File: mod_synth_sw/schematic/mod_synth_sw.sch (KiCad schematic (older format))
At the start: 43 parts, among them J1 Conn_02x08_Odd_Even, J2 CLK, J3 RST, J4 I/O, J5 I/O 1, J6 I/O 2, J7 I/O 3, J8 I/O 4, Q1 2N3904, Q2 2N3904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

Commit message: Layout some tracks
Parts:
- added C2, C3, C4: 100nf, Capacitor_THT:C_Disc_D9.0mm_W2.5mm_P5.00mm, symbol Device:C_Small
- added C5, C6: 10uf, Capacitor_THT:CP_Radial_D5.0mm_P2.00mm, symbol Device:CP_Small
- added J10, J9: Conn_01x05_Female, Connector_PinSocket_2.54mm:PinSocket_1x05_P2.54mm_Vertical, symbol Connector:Conn_01x05_Female
- added J11, J12: Conn_01x05_Male, Connector_PinHeader_2.54mm:PinHeader_1x05_P2.54mm_Vertical, symbol Connector:Conn_01x05_Male
- U1: footprint Package_DIP:DIP-16_W7.62mm -> Package_DIP:DIP-16_W7.62mm_Socket_LongPads
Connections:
- net +12V: now also J1.10 (Pin_10), J1.9 (Pin_9), U1.13 (V+), U2.16 (VDD), C2.2, C4.2, C6.1
- net GND: now also J1.3 (Pin_3), J1.5 (Pin_5), J1.7 (Pin_7), U1.5 (GND), U2.8 (VSS), C2.1, C3.2, C4.1, C5.1, C6.2, J10.1 (Pin_1); no longer J2.S, J3.S, J4.S, J5.S, J6.S, J7.S, J8.S, R10.1
- net -12V: now reaches J1.1 (Pin_1)
- net -12V: now also J1.2 (Pin_2), U1.4 (V-), C3.1, C5.2
- net at J1.4 (Pin_4): now also J1.6 (Pin_6), J1.8 (Pin_8)
- new net GND_PCB_B: J12.1 (Pin_1), J2.S, J3.S, J4.S, J5.S, J6.S, J7.S, J8.S, R10.1

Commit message: Enlarge second PCB
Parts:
- J10: renamed from J11; value Conn_01x05_Male -> Conn_01x06_Male; footprint Connector_PinHeader_2.54mm:PinHeader_1x05_P2.54mm_Vertical -> Connector_PinHeader_2.54mm:PinHeader_1x06_P2.54mm_Vertical; symbol Connector:Conn_01x05_Male -> Connector:Conn_01x06_Male
- J11: renamed from J10; value Conn_01x05_Female -> Conn_01x07_Female; footprint Connector_PinSocket_2.54mm:PinSocket_1x05_P2.54mm_Vertical -> Connector_PinSocket_2.54mm:PinSocket_1x07_P2.54mm_Vertical; symbol Connector:Conn_01x05_Female -> Connector:Conn_01x07_Female
- J12: value Conn_01x05_Male -> Conn_01x07_Male; footprint Connector_PinHeader_2.54mm:PinHeader_1x05_P2.54mm_Vertical -> Connector_PinHeader_2.54mm:PinHeader_1x07_P2.54mm_Vertical; symbol Connector:Conn_01x05_Male -> Connector:Conn_01x07_Male
- J9: value Conn_01x05_Female -> Conn_01x06_Female; footprint Connector_PinSocket_2.54mm:PinSocket_1x05_P2.54mm_Vertical -> Connector_PinSocket_2.54mm:PinSocket_1x06_P2.54mm_Vertical; symbol Connector:Conn_01x05_Female -> Connector:Conn_01x06_Female
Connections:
- net GND: now also J1.4 (Pin_4), J1.6 (Pin_6), J1.8 (Pin_8)
- net SW_RST_PCB_A: now reaches D3.1 (K), D4.1 (K), D5.1 (K), R8.1, U2.15 (Reset)
- net SW_RST_PCB_A: no longer D6.1 (K)
- net LED_2_PCB_A: now reaches U1.8, U2.2 (Q1)
- net LED_2_PCB_A: now also J11.2 (Pin_2); no longer D8.2 (A)
- net LED_1_PCB_A: now reaches U1.1, U2.3 (Q0)
- net LED_1_PCB_A: now also J9.5 (Pin_5); no longer D7.2 (A)
- net LED_3_PCB_A: now reaches U1.9, U2.4 (Q2)
- net LED_3_PCB_A: now also J11.4 (Pin_4); no longer D9.2 (A), SW3.3
- net LED_4_PCB_A: now reaches U1.16, U2.7 (Q3)
- net LED_4_PCB_A: now also J11.6 (Pin_6); no longer D10.2 (A), SW3.1
- net 1_PCB_A: now reaches U1.3
- net 1_PCB_A: now also J9.6 (Pin_6); no longer R12.2
- net 2_PCB_A: now reaches U1.7
- net 2_PCB_A: now also J11.3 (Pin_3); no longer R13.2
- net 3_PCB_A: now reaches U1.11
- net 3_PCB_A: now also J11.5 (Pin_5); no longer R14.2
- net 4_PCB_A: now reaches U1.14
- net 4_PCB_A: now also J11.7 (Pin_7); no longer R15.2
- net 0_PCB_A: now reaches U1.10, U1.15, U1.2, U1.6
- net 0_PCB_A: now also J9.4 (Pin_4); no longer R11.2
- net CLK_PCB_A: now reaches Q1.2 (B)
- net CLK_PCB_A: no longer R1.1
- net RST_PCB_A: now reaches Q2.2 (B)
- net RST_PCB_A: no longer R2.1
- net 0_PCB_B: now reaches J10.4 (Pin_4)
- net 0_PCB_B: now also R11.2
- net LED_1_PCB_B: now reaches J10.5 (Pin_5)
- net LED_1_PCB_B: now also D7.2 (A)
- net LED_2_PCB_B: now reaches J12.2 (Pin_2)
- net LED_2_PCB_B: now also D8.2 (A)
- net 2_PCB_B: now reaches J12.3 (Pin_3)
- net 2_PCB_B: now also R13.2
- net LED_3_PCB_B: now reaches J12.4 (Pin_4)
- net LED_3_PCB_B: now also D9.2 (A), SW3.3
- net 3_PCB_B: now reaches J12.5 (Pin_5)
- net 3_PCB_B: now also R14.2
- new net 1_PCB_B: J10.6 (Pin_6), R12.2
- new net 4_PCB_B: J12.7 (Pin_7), R15.2
- new net CLK_PCB_B: R1.1
- new net LED_4_PCB_B: D10.2 (A), J12.6 (Pin_6), SW3.1
- new net RST_PCB_B: R2.1
- new net SW_RST_PCB_B: D6.1 (K)
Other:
- moved on the sheet: D10, D6, D7, D8, D9, J2, J3, R1, R10, R2, SW3

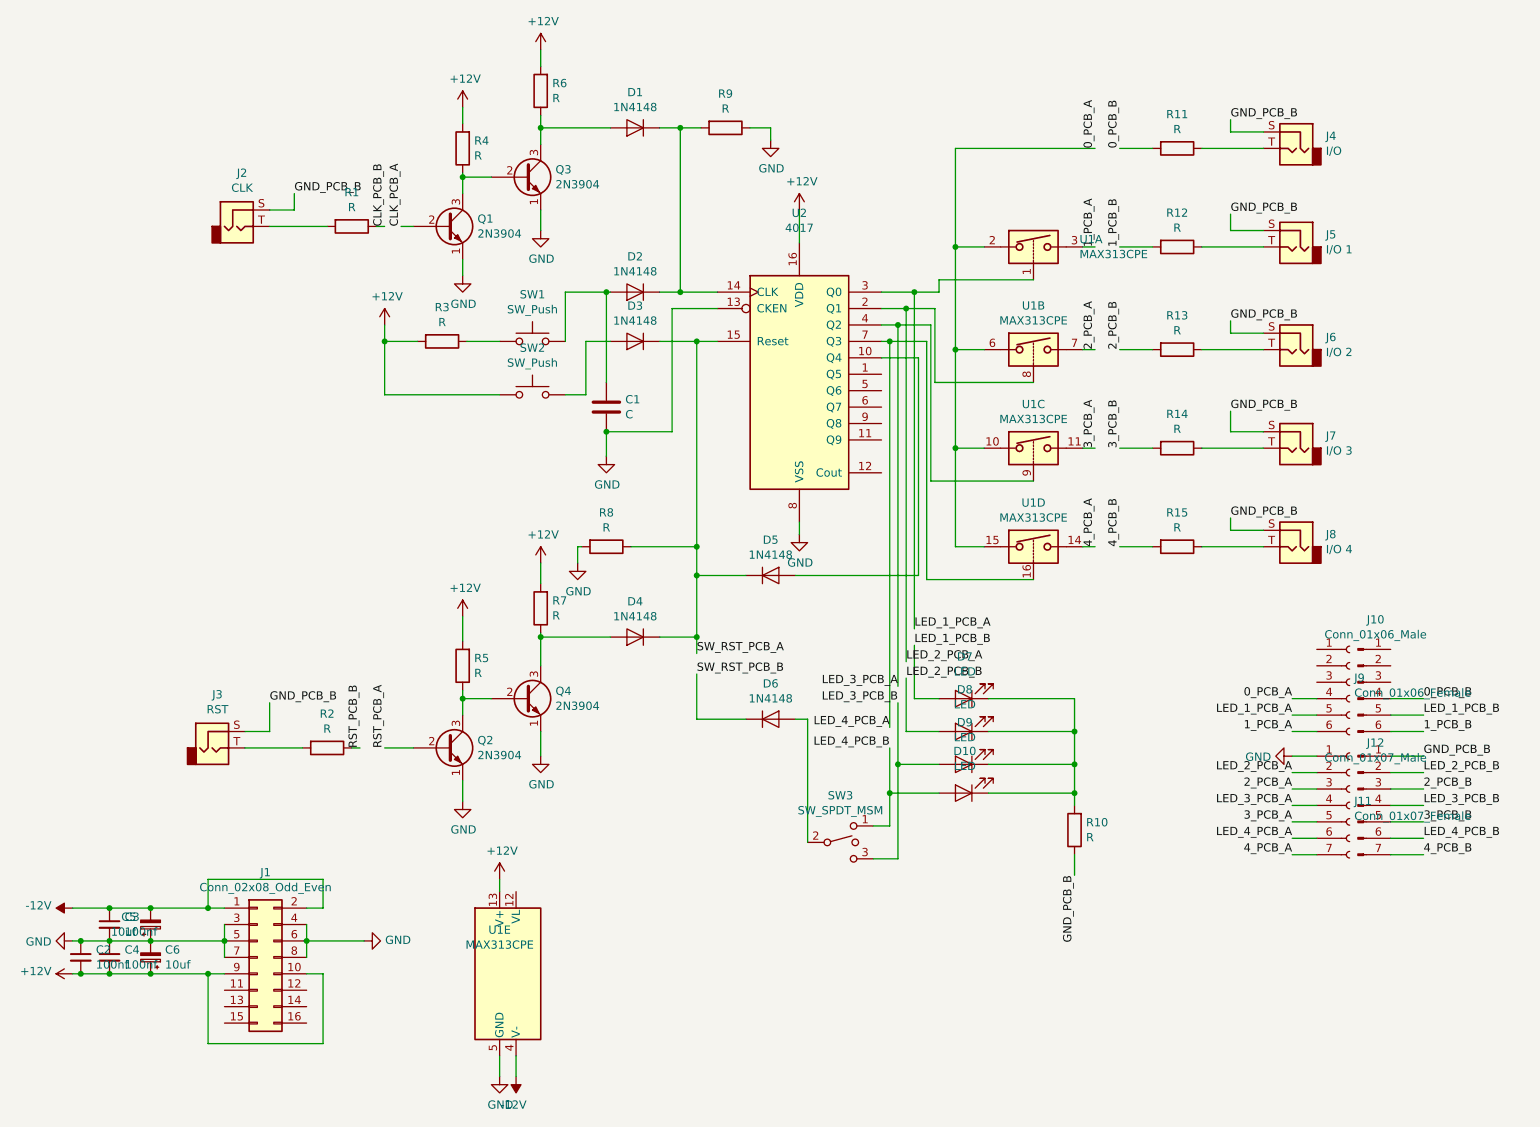
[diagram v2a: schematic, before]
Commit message: Add missing connections
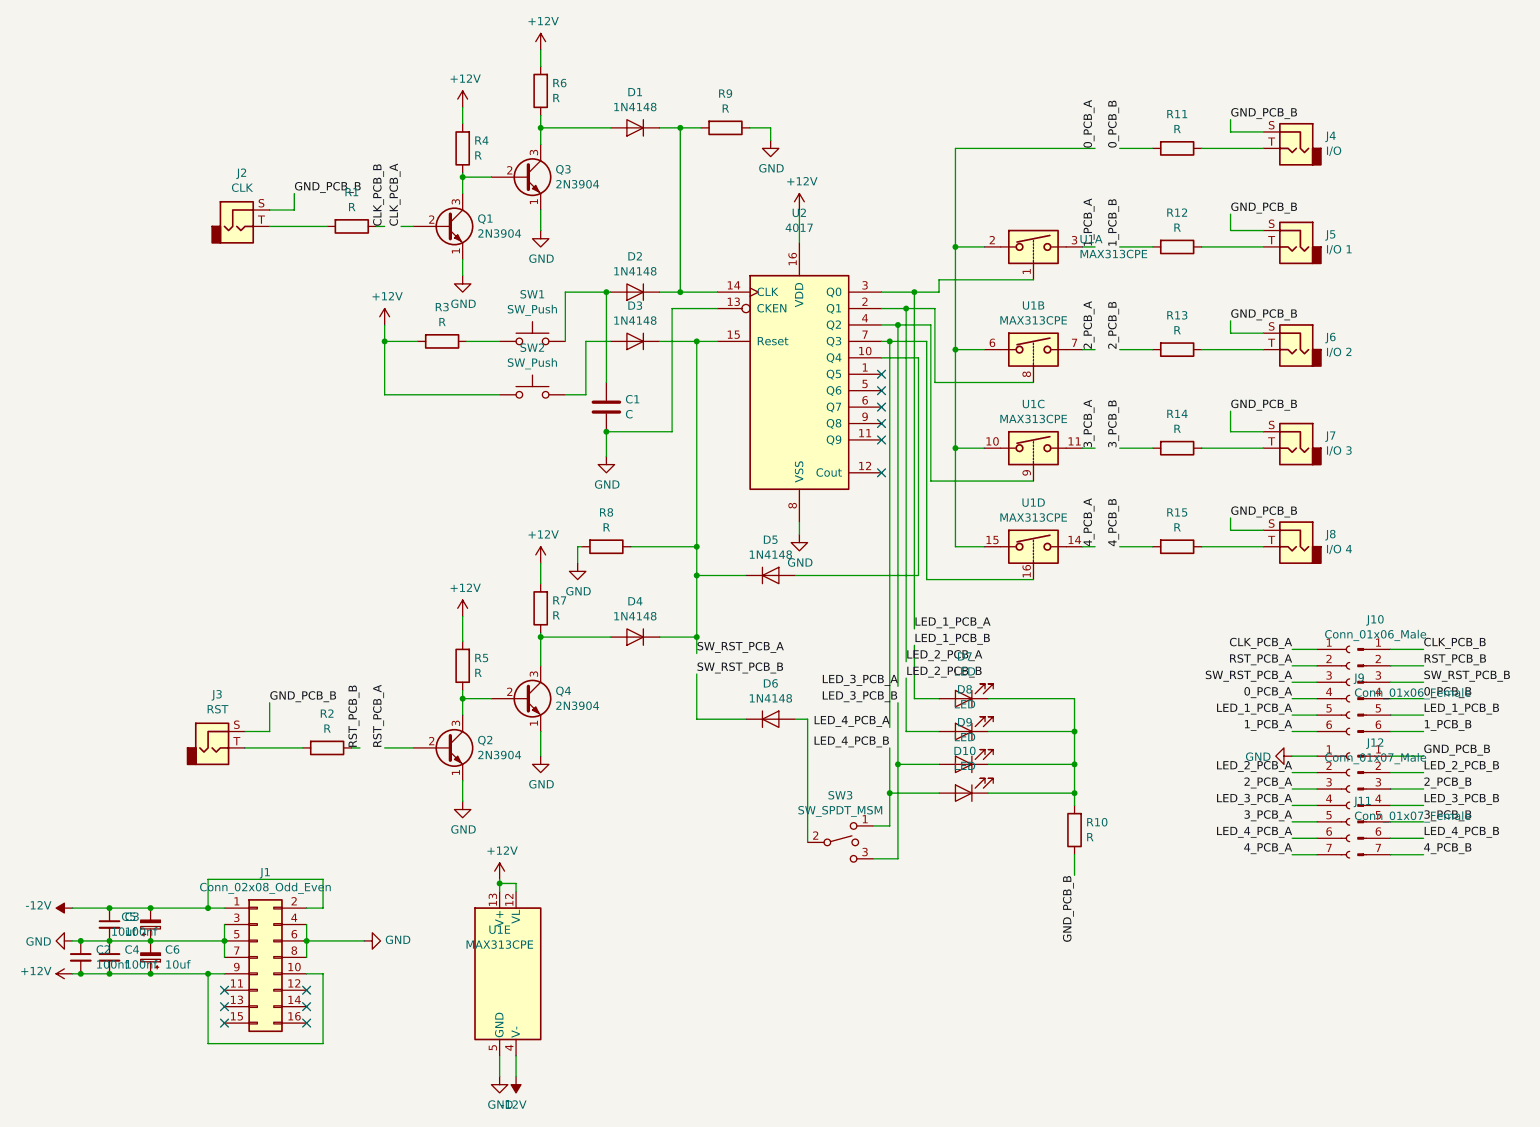
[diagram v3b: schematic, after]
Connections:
- net +12V: now also U1.12 (VL)
- net CLK_PCB_A: now also J9.1 (Pin_1)
- net CLK_PCB_B: now also J10.1 (Pin_1)
- net RST_PCB_A: now also J9.2 (Pin_2)
- net RST_PCB_B: now also J10.2 (Pin_2)
- net SW_RST_PCB_A: now also J9.3 (Pin_3)
- net SW_RST_PCB_B: now also J10.3 (Pin_3)
- no-connect marks 0 -> 12
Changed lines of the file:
@@
 $EndComp
 Wire Wire Line
-	3525 6125 3525 6200
+	3525 6125 3525 6150
 Wire Wire Line
 	3525 7200 3525 7325
@@
 LED_2_PCB_B
 $Comp
-L power:GND #PWR?
+L power:GND #PWR0103
 U 1 1 5D8A7916
 P 2700 6500
-F 0 "#PWR?" H 2700 6250 50  0001 C CNN
+F 0 "#PWR0103" H 2700 6250 50  0001 C CNN
 F 1 "GND" V 2705 6372 50  0000 R CNN
 F 2 "" H 2700 6500 50  0001 C CNN
@@
 Wire Wire Line
 	8950 5025 9150 5025
+Text Label 8350 4725 2    50   ~ 0
+CLK_PCB_A
+Text Label 8350 4825 2    50   ~ 0
+RST_PCB_A
+Text Label 8350 4925 2    50   ~ 0
+SW_RST_PCB_A
+Text Label 9150 4725 0    50   ~ 0
+CLK_PCB_B
+Text Label 9150 4825 0    50   ~ 0
+RST_PCB_B
+Text Label 9150 4925 0    50   ~ 0
+SW_RST_PCB_B
+Wire Wire Line
+	8350 4725 8500 4725
+Wire Wire Line
+	8500 4825 8350 4825
+Wire Wire Line
+	8350 4925 8500 4925
+Wire Wire Line
+	8950 4725 9150 4725
+Wire Wire Line
+	9150 4825 8950 4825
+Wire Wire Line
+	8950 4925 9150 4925
+NoConn ~ 5850 3650
+NoConn ~ 5850 3450
+NoConn ~ 5850 3350
+NoConn ~ 5850 3250
+NoConn ~ 5850 3150
+NoConn ~ 5850 3050
+Wire Wire Line
+	3525 6150 3625 6150
+Wire Wire Line
+	3625 6150 3625 6200
+Connection ~ 3525 6150
+Wire Wire Line
+	3525 6150 3525 6200
+NoConn ~ 2350 6800
+NoConn ~ 2350 6900
+NoConn ~ 2350 7000
+NoConn ~ 1850 7000
+NoConn ~ 1850 6900
+NoConn ~ 1850 6800
 $EndSCHEMATC

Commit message: Update values
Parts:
- C1: value C -> 100n
- R1, R2, R8, R9: value R -> 47k
- R10: value R -> 2k7
- R11, R12, R13, R14, R15: value R -> 1k
- R3, R4, R5, R6, R7: value R -> 10k
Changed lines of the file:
@@
 P 7650 2275
 F 0 "R12" V 7443 2275 50  0000 C CNN
-F 1 "R" V 7534 2275 50  0000 C CNN
+F 1 "1k" V 7534 2275 50  0000 C CNN
 F 2 "Resistor_THT:R_Axial_DIN0207_L6.3mm_D2.5mm_P10.16mm_Horizontal" V 7580 2275 50  0001 C CNN
 F 3 "~" H 7650 2275 50  0001 C CNN
@@
 P 7650 2900
 F 0 "R13" V 7443 2900 50  0000 C CNN
-F 1 "R" V 7534 2900 50  0000 C CNN
+F 1 "1k" V 7534 2900 50  0000 C CNN
 F 2 "Resistor_THT:R_Axial_DIN0207_L6.3mm_D2.5mm_P10.16mm_Horizontal" V 7580 2900 50  0001 C CNN
 F 3 "~" H 7650 2900 50  0001 C CNN
@@
 P 7650 3500
 F 0 "R14" V 7443 3500 50  0000 C CNN
-F 1 "R" V 7534 3500 50  0000 C CNN
+F 1 "1k" V 7534 3500 50  0000 C CNN
 F 2 "Resistor_THT:R_Axial_DIN0207_L6.3mm_D2.5mm_P10.16mm_Horizontal" V 7580 3500 50  0001 C CNN
 F 3 "~" H 7650 3500 50  0001 C CNN
@@
 P 7650 4100
 F 0 "R15" V 7443 4100 50  0000 C CNN
-F 1 "R" V 7534 4100 50  0000 C CNN
+F 1 "1k" V 7534 4100 50  0000 C CNN
 F 2 "Resistor_THT:R_Axial_DIN0207_L6.3mm_D2.5mm_P10.16mm_Horizontal" V 7580 4100 50  0001 C CNN
 F 3 "~" H 7650 4100 50  0001 C CNN
@@
 P 7650 1675
 F 0 "R11" V 7443 1675 50  0000 C CNN
-F 1 "R" V 7534 1675 50  0000 C CNN
+F 1 "1k" V 7534 1675 50  0000 C CNN
 F 2 "Resistor_THT:R_Axial_DIN0207_L6.3mm_D2.5mm_P10.16mm_Horizontal" V 7580 1675 50  0001 C CNN
 F 3 "~" H 7650 1675 50  0001 C CNN
@@
 P 2625 2150
 F 0 "R1" V 2418 2150 50  0000 C CNN
-F 1 "R" V 2509 2150 50  0000 C CNN
+F 1 "47k" V 2509 2150 50  0000 C CNN
 F 2 "Resistor_THT:R_Axial_DIN0207_L6.3mm_D2.5mm_P10.16mm_Horizontal" V 2555 2150 50  0001 C CNN
 F 3 "~" H 2625 2150 50  0001 C CNN
@@
 P 2475 5325
 F 0 "R2" V 2268 5325 50  0000 C CNN
-F 1 "R" V 2359 5325 50  0000 C CNN
+F 1 "47k" V 2359 5325 50  0000 C CNN
 F 2 "Resistor_THT:R_Axial_DIN0207_L6.3mm_D2.5mm_P10.16mm_Horizontal" V 2405 5325 50  0001 C CNN
 F 3 "~" H 2475 5325 50  0001 C CNN
@@
 P 3300 4825
 F 0 "R5" H 3230 4779 50  0000 R CNN
-F 1 "R" H 3230 4870 50  0000 R CNN
+F 1 "10k" H 3230 4870 50  0000 R CNN
 F 2 "Resistor_THT:R_Axial_DIN0207_L6.3mm_D2.5mm_P10.16mm_Horizontal" V 3230 4825 50  0001 C CNN
 F 3 "~" H 3300 4825 50  0001 C CNN
@@
 P 3775 4475
 F 0 "R7" H 3705 4429 50  0000 R CNN
-F 1 "R" H 3705 4520 50  0000 R CNN
+F 1 "10k" H 3705 4520 50  0000 R CNN
 F 2 "Resistor_THT:R_Axial_DIN0207_L6.3mm_D2.5mm_P10.16mm_Horizontal" V 3705 4475 50  0001 C CNN
 F 3 "~" H 3775 4475 50  0001 C CNN
@@
 P 3300 1675
 F 0 "R4" H 3230 1629 50  0000 R CNN
-F 1 "R" H 3230 1720 50  0000 R CNN
+F 1 "10k" H 3230 1720 50  0000 R CNN
 F 2 "Resistor_THT:R_Axial_DIN0207_L6.3mm_D2.5mm_P10.16mm_Horizontal" V 3230 1675 50  0001 C CNN
 F 3 "~" H 3300 1675 50  0001 C CNN
@@
 P 3775 1325
 F 0 "R6" H 3705 1279 50  0000 R CNN
-F 1 "R" H 3705 1370 50  0000 R CNN
+F 1 "10k" H 3705 1370 50  0000 R CNN
 F 2 "Resistor_THT:R_Axial_DIN0207_L6.3mm_D2.5mm_P10.16mm_Horizontal" V 3705 1325 50  0001 C CNN
 F 3 "~" H 3775 1325 50  0001 C CNN
@@
 P 4900 1550
 F 0 "R9" V 4693 1550 50  0000 C CNN
-F 1 "R" V 4784 1550 50  0000 C CNN
+F 1 "47k" V 4784 1550 50  0000 C CNN
 F 2 "Resistor_THT:R_Axial_DIN0207_L6.3mm_D2.5mm_P10.16mm_Horizontal" V 4830 1550 50  0001 C CNN
 F 3 "~" H 4900 1550 50  0001 C CNN
@@
 P 4175 4100
 F 0 "R8" V 3968 4100 50  0000 C CNN
-F 1 "R" V 4059 4100 50  0000 C CNN
+F 1 "47k" V 4059 4100 50  0000 C CNN
 F 2 "Resistor_THT:R_Axial_DIN0207_L6.3mm_D2.5mm_P10.16mm_Horizontal" V 4105 4100 50  0001 C CNN
 F 3 "~" H 4175 4100 50  0001 C CNN
@@
 P 7025 5825
 F 0 "R10" H 6955 5779 50  0000 R CNN
-F 1 "R" H 6955 5870 50  0000 R CNN
+F 1 "2k7" H 6955 5870 50  0000 R CNN
 F 2 "Resistor_THT:R_Axial_DIN0207_L6.3mm_D2.5mm_P10.16mm_Horizontal" V 6955 5825 50  0001 C CNN
 F 3 "~" H 7025 5825 50  0001 C CNN
@@
 P 3175 2850
 F 0 "R3" V 2968 2850 50  0000 C CNN
-F 1 "R" V 3059 2850 50  0000 C CNN
+F 1 "10k" V 3059 2850 50  0000 C CNN
 F 2 "Resistor_THT:R_Axial_DIN0207_L6.3mm_D2.5mm_P10.16mm_Horizontal" V 3105 2850 50  0001 C CNN
 F 3 "~" H 3175 2850 50  0001 C CNN
@@
 P 4175 3250
 F 0 "C1" H 4290 3296 50  0000 L CNN
-F 1 "C" H 4290 3205 50  0000 L CNN
+F 1 "100n" H 4290 3205 50  0000 L CNN
 F 2 "Capacitor_THT:C_Disc_D9.0mm_W2.5mm_P5.00mm" H 4213 3100 50  0001 C CNN
 F 3 "~" H 4175 3250 50  0001 C CNN
